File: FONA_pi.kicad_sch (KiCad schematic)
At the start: 2 parts, among them J1 Conn_01x20_Socket, J2 Conn_01x20_Socket

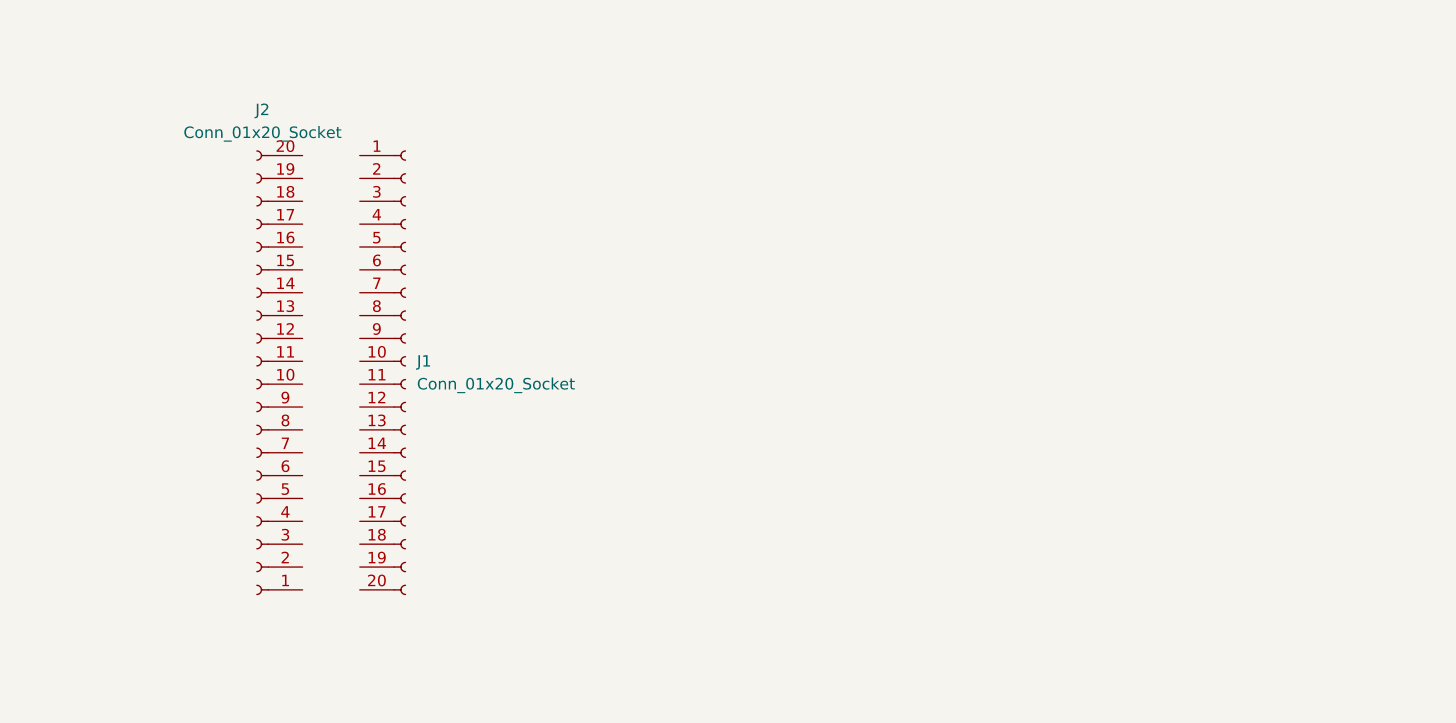
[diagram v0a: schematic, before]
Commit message: Added some 1x20 to schematic
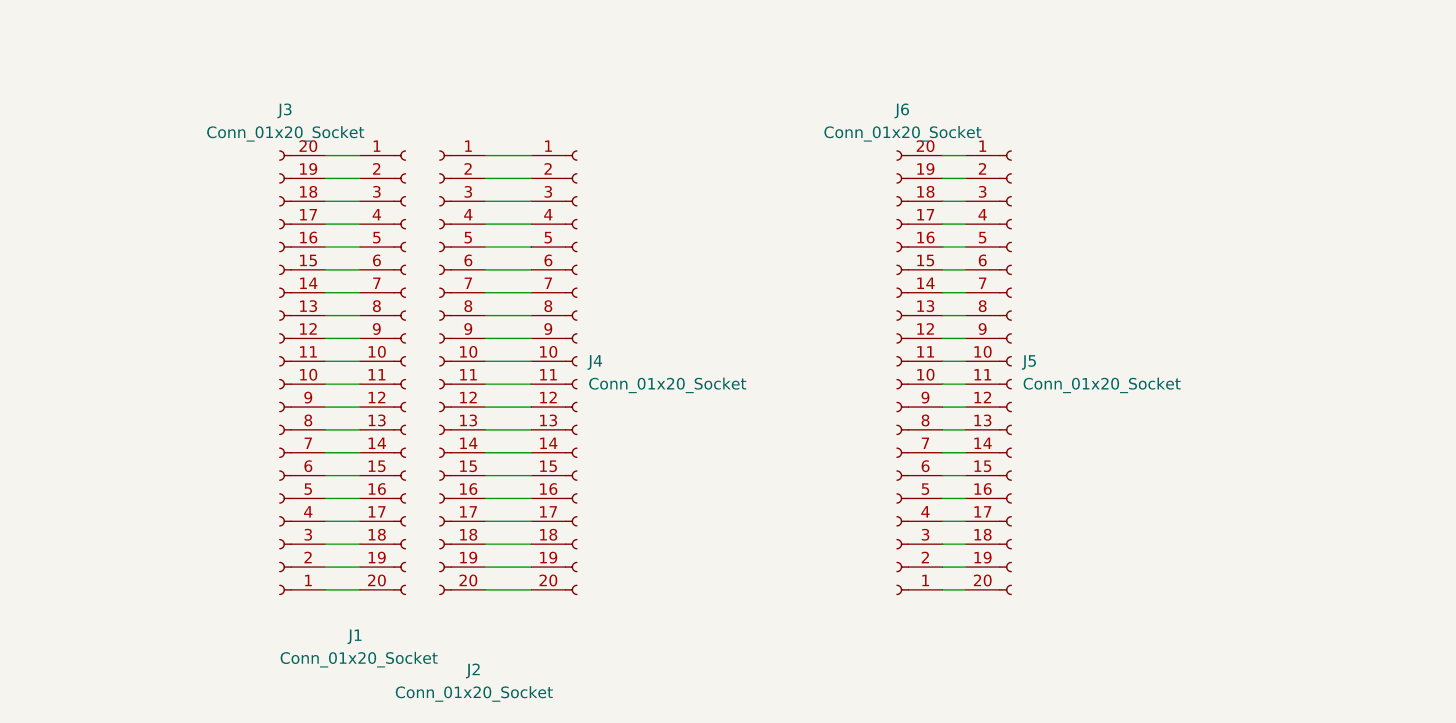
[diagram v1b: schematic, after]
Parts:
- added J3, J4, J5, J6: Conn_01x20_Socket, Connector_PinSocket_2.54mm:PinSocket_1x20_P2.54mm_Vertical, symbol Connector:Conn_01x20_Socket
- J1, J2: footprint (none) -> Connector_PinHeader_2.54mm:PinHeader_1x20_P2.54mm_Vertical
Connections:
- net at J2.1 (Pin_1): now also J4.1 (Pin_1)
- net at J2.10 (Pin_10): now also J4.10 (Pin_10)
- net at J2.11 (Pin_11): now also J4.11 (Pin_11)
- net at J2.12 (Pin_12): now also J4.12 (Pin_12)
- net at J2.13 (Pin_13): now also J4.13 (Pin_13)
- net at J2.14 (Pin_14): now also J4.14 (Pin_14)
- net at J2.15 (Pin_15): now also J4.15 (Pin_15)
- net at J2.16 (Pin_16): now also J4.16 (Pin_16)
- net at J2.17 (Pin_17): now also J4.17 (Pin_17)
- net at J2.18 (Pin_18): now also J4.18 (Pin_18)
- net at J2.19 (Pin_19): now also J4.19 (Pin_19)
- net at J2.2 (Pin_2): now also J4.2 (Pin_2)
- net at J2.20 (Pin_20): now also J4.20 (Pin_20)
- net at J2.3 (Pin_3): now also J4.3 (Pin_3)
- net at J2.4 (Pin_4): now also J4.4 (Pin_4)
- net at J2.5 (Pin_5): now also J4.5 (Pin_5)
- net at J2.6 (Pin_6): now also J4.6 (Pin_6)
- net at J2.7 (Pin_7): now also J4.7 (Pin_7)
- net at J2.8 (Pin_8): now also J4.8 (Pin_8)
- net at J2.9 (Pin_9): now also J4.9 (Pin_9)
- net at J1.1 (Pin_1): now also J3.20 (Pin_20)
- net at J1.10 (Pin_10): now also J3.11 (Pin_11)
- net at J1.11 (Pin_11): now also J3.10 (Pin_10)
- net at J1.12 (Pin_12): now also J3.9 (Pin_9)
- net at J1.13 (Pin_13): now also J3.8 (Pin_8)
- net at J1.14 (Pin_14): now also J3.7 (Pin_7)
- net at J1.15 (Pin_15): now also J3.6 (Pin_6)
- net at J1.16 (Pin_16): now also J3.5 (Pin_5)
- net at J1.17 (Pin_17): now also J3.4 (Pin_4)
- net at J1.18 (Pin_18): now also J3.3 (Pin_3)
- net at J1.19 (Pin_19): now also J3.2 (Pin_2)
- net at J1.2 (Pin_2): now also J3.19 (Pin_19)
- net at J1.20 (Pin_20): now also J3.1 (Pin_1)
- net at J1.3 (Pin_3): now also J3.18 (Pin_18)
- net at J1.4 (Pin_4): now also J3.17 (Pin_17)
- net at J1.5 (Pin_5): now also J3.16 (Pin_16)
- net at J1.6 (Pin_6): now also J3.15 (Pin_15)
- net at J1.7 (Pin_7): now also J3.14 (Pin_14)
- net at J1.8 (Pin_8): now also J3.13 (Pin_13)
- net at J1.9 (Pin_9): now also J3.12 (Pin_12)
- new net: J5.20 (Pin_20), J6.1 (Pin_1)
- new net: J5.11 (Pin_11), J6.10 (Pin_10)
- new net: J5.10 (Pin_10), J6.11 (Pin_11)
- new net: J5.9 (Pin_9), J6.12 (Pin_12)
- new net: J5.8 (Pin_8), J6.13 (Pin_13)
- new net: J5.7 (Pin_7), J6.14 (Pin_14)
- new net: J5.6 (Pin_6), J6.15 (Pin_15)
- new net: J5.5 (Pin_5), J6.16 (Pin_16)
- new net: J5.4 (Pin_4), J6.17 (Pin_17)
- new net: J5.3 (Pin_3), J6.18 (Pin_18)
- new net: J5.2 (Pin_2), J6.19 (Pin_19)
- new net: J5.19 (Pin_19), J6.2 (Pin_2)
- new net: J5.1 (Pin_1), J6.20 (Pin_20)
- new net: J5.18 (Pin_18), J6.3 (Pin_3)
- new net: J5.17 (Pin_17), J6.4 (Pin_4)
- new net: J5.16 (Pin_16), J6.5 (Pin_5)
- new net: J5.15 (Pin_15), J6.6 (Pin_6)
- new net: J5.14 (Pin_14), J6.7 (Pin_7)
- new net: J5.13 (Pin_13), J6.8 (Pin_8)
- new net: J5.12 (Pin_12), J6.9 (Pin_9)
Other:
- moved on the sheet: J2

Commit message: connections for pi and fona
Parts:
- added J7: Conn_01x20_Socket, Connector_PinHeader_2.00mm:PinHeader_1x20_P2.00mm_Vertical, symbol Connector:Conn_01x20_Socket
- J3: value Conn_01x20_Socket -> Outer_Pi_01x20_Socket
- J4: value Conn_01x20_Socket -> Inner_Pi_01x20_Socket
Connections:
- net at J5.20 (Pin_20), J6.1 (Pin_1): now also J7.1 (Pin_1)
- net at J5.11 (Pin_11), J6.10 (Pin_10): now also J7.10 (Pin_10)
- net at J5.10 (Pin_10), J6.11 (Pin_11): now also J7.11 (Pin_11)
- net at J5.9 (Pin_9), J6.12 (Pin_12): now also J7.12 (Pin_12)
- net at J5.8 (Pin_8), J6.13 (Pin_13): now also J7.13 (Pin_13)
- net at J5.7 (Pin_7), J6.14 (Pin_14): now also J7.14 (Pin_14)
- net at J5.6 (Pin_6), J6.15 (Pin_15): now also J7.15 (Pin_15)
- net at J5.5 (Pin_5), J6.16 (Pin_16): now also J7.16 (Pin_16)
- net at J5.4 (Pin_4), J6.17 (Pin_17): now also J7.17 (Pin_17)
- net at J5.3 (Pin_3), J6.18 (Pin_18): now also J7.18 (Pin_18)
- net at J5.2 (Pin_2), J6.19 (Pin_19): now also J7.19 (Pin_19)
- net at J5.19 (Pin_19), J6.2 (Pin_2): now also J7.2 (Pin_2)
- net at J5.1 (Pin_1), J6.20 (Pin_20): now also J7.20 (Pin_20)
- net at J5.18 (Pin_18), J6.3 (Pin_3): now also J7.3 (Pin_3)
- net at J5.17 (Pin_17), J6.4 (Pin_4): now also J7.4 (Pin_4)
- net at J5.16 (Pin_16), J6.5 (Pin_5): now also J7.5 (Pin_5)
- net at J5.15 (Pin_15), J6.6 (Pin_6): now also J7.6 (Pin_6)
- net at J5.14 (Pin_14), J6.7 (Pin_7): now also J7.7 (Pin_7)
- net at J5.13 (Pin_13), J6.8 (Pin_8): now also J7.8 (Pin_8)
- net at J5.12 (Pin_12), J6.9 (Pin_9): now also J7.9 (Pin_9)

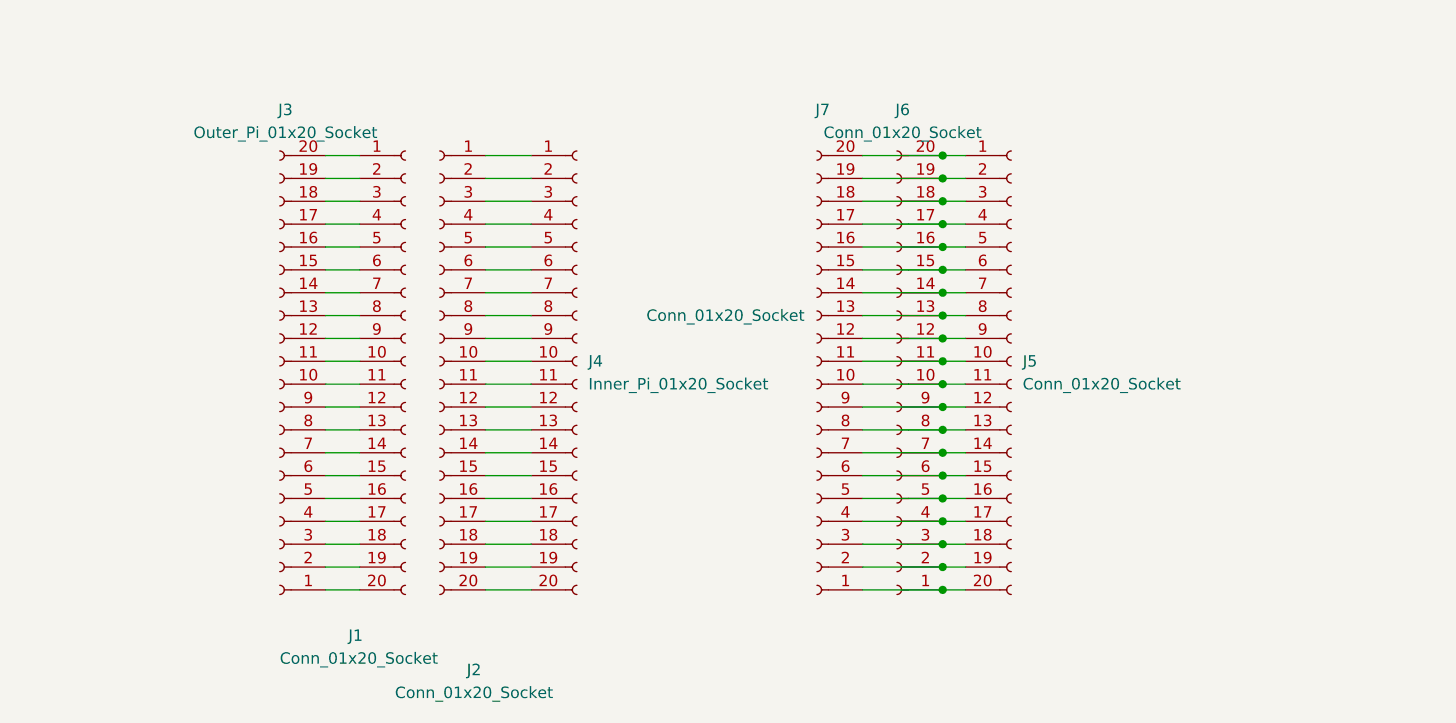
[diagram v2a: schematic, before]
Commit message: Flipped all the sockets so the pins are all aligned the same with square holes at the top, sch and pcb
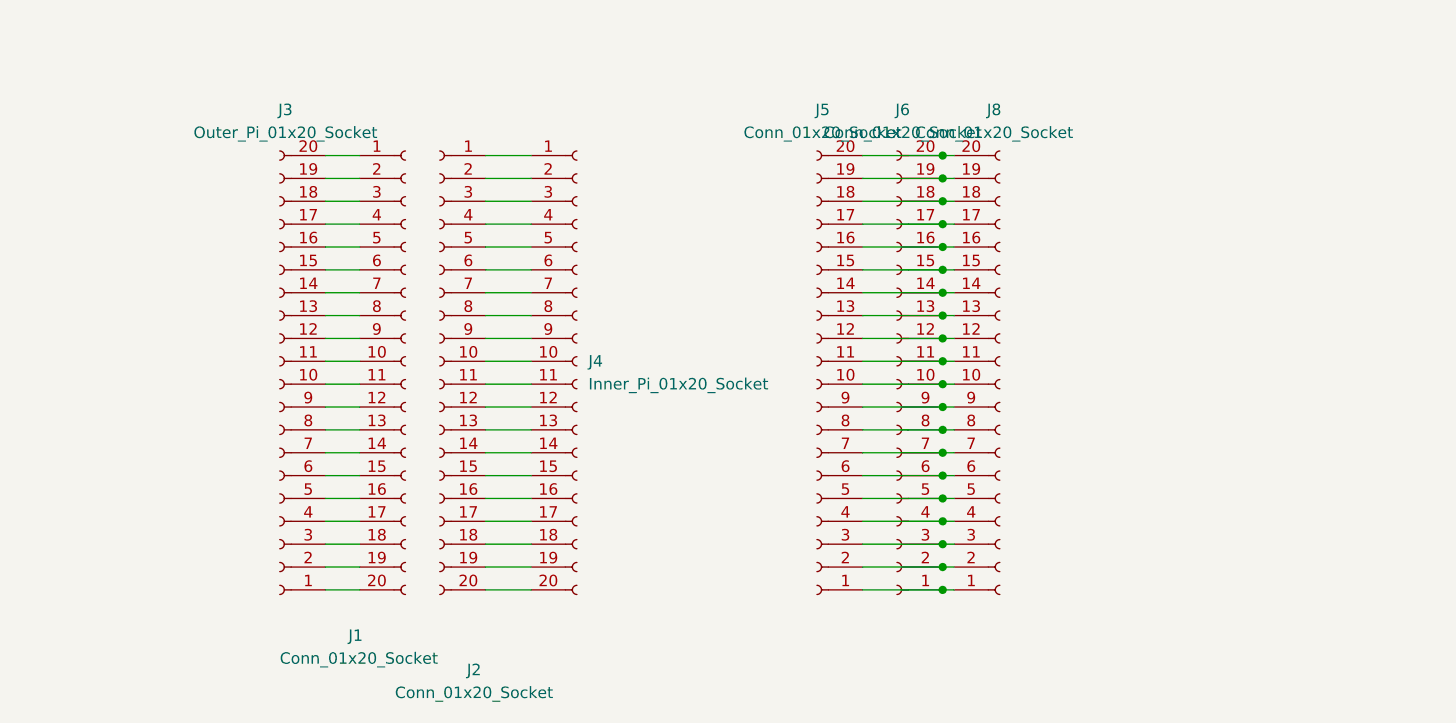
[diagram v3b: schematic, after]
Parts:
- removed J7: Conn_01x20_Socket, Connector_PinHeader_2.00mm:PinHeader_1x20_P2.00mm_Vertical, symbol Connector:Conn_01x20_Socket
- added J8: Conn_01x20_Socket, Connector_PinHeader_2.54mm:PinHeader_1x20_P2.54mm_Vertical, symbol Connector:Conn_01x20_Socket
- J5: footprint Connector_PinSocket_2.54mm:PinSocket_1x20_P2.54mm_Vertical -> Connector_PinHeader_2.54mm:PinHeader_1x20_P2.54mm_Vertical
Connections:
- net at J6.1 (Pin_1): now also J5.1 (Pin_1), J8.1 (Pin_1); no longer J5.20 (Pin_20)
- net at J6.10 (Pin_10): now also J5.10 (Pin_10), J8.10 (Pin_10); no longer J5.11 (Pin_11)
- net at J6.11 (Pin_11): now also J5.11 (Pin_11), J8.11 (Pin_11); no longer J5.10 (Pin_10)
- net at J6.12 (Pin_12): now also J5.12 (Pin_12), J8.12 (Pin_12); no longer J5.9 (Pin_9)
- net at J6.13 (Pin_13): now also J5.13 (Pin_13), J8.13 (Pin_13); no longer J5.8 (Pin_8)
- net at J6.14 (Pin_14): now also J5.14 (Pin_14), J8.14 (Pin_14); no longer J5.7 (Pin_7)
- net at J6.15 (Pin_15): now also J5.15 (Pin_15), J8.15 (Pin_15); no longer J5.6 (Pin_6)
- net at J6.16 (Pin_16): now also J5.16 (Pin_16), J8.16 (Pin_16); no longer J5.5 (Pin_5)
- net at J6.17 (Pin_17): now also J5.17 (Pin_17), J8.17 (Pin_17); no longer J5.4 (Pin_4)
- net at J6.18 (Pin_18): now also J5.18 (Pin_18), J8.18 (Pin_18); no longer J5.3 (Pin_3)
- net at J6.19 (Pin_19): now also J5.19 (Pin_19), J8.19 (Pin_19); no longer J5.2 (Pin_2)
- net at J6.2 (Pin_2): now also J5.2 (Pin_2), J8.2 (Pin_2); no longer J5.19 (Pin_19)
- net at J6.20 (Pin_20): now also J5.20 (Pin_20), J8.20 (Pin_20); no longer J5.1 (Pin_1)
- net at J6.3 (Pin_3): now also J5.3 (Pin_3), J8.3 (Pin_3); no longer J5.18 (Pin_18)
- net at J6.4 (Pin_4): now also J5.4 (Pin_4), J8.4 (Pin_4); no longer J5.17 (Pin_17)
- net at J6.5 (Pin_5): now also J5.5 (Pin_5), J8.5 (Pin_5); no longer J5.16 (Pin_16)
- net at J6.6 (Pin_6): now also J5.6 (Pin_6), J8.6 (Pin_6); no longer J5.15 (Pin_15)
- net at J6.7 (Pin_7): now also J5.7 (Pin_7), J8.7 (Pin_7); no longer J5.14 (Pin_14)
- net at J6.8 (Pin_8): now also J5.8 (Pin_8), J8.8 (Pin_8); no longer J5.13 (Pin_13)
- net at J6.9 (Pin_9): now also J5.9 (Pin_9), J8.9 (Pin_9); no longer J5.12 (Pin_12)

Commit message: Got rid of the headers in 3D viewer.  Cleaned up pin headers.  Using 40-pin Rpi header
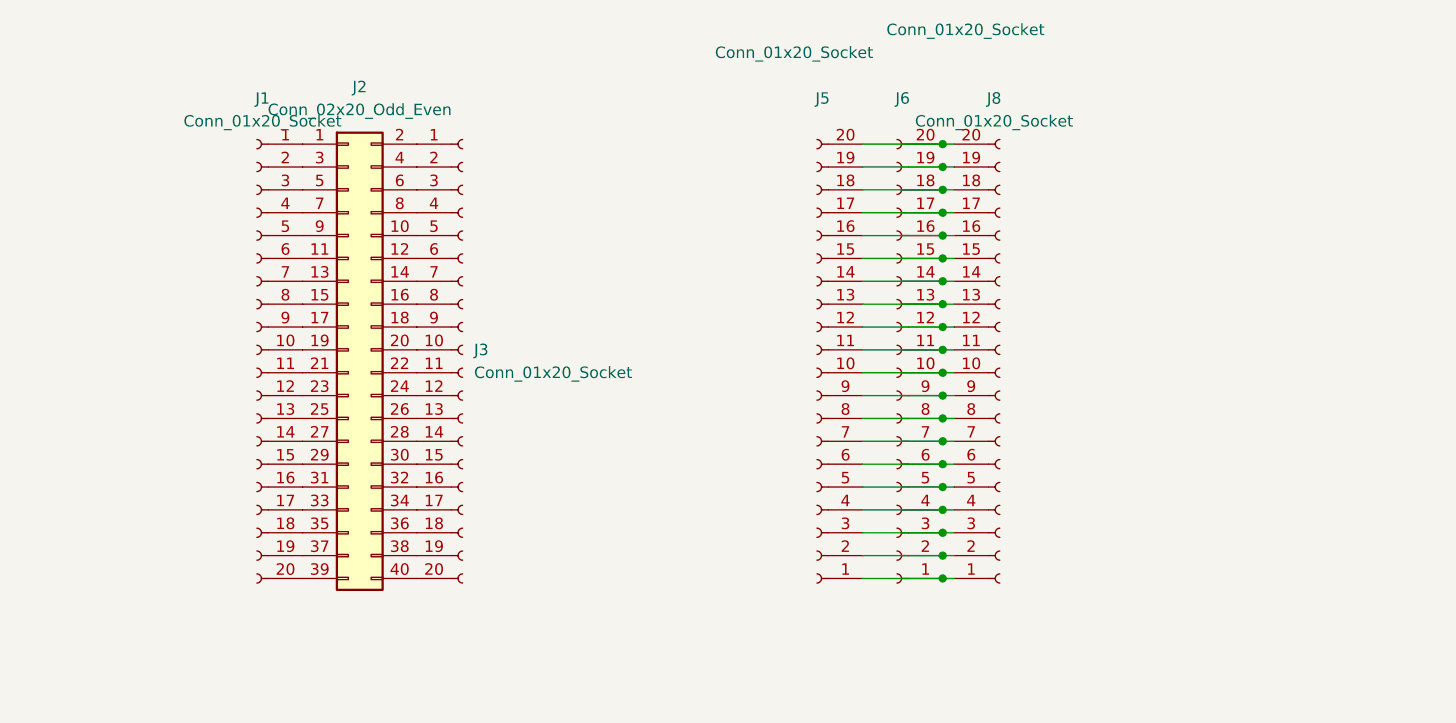
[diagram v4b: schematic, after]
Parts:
- removed J2: Conn_01x20_Socket, Connector_PinHeader_2.54mm:PinHeader_1x20_P2.54mm_Vertical, symbol Connector:Conn_01x20_Socket
- removed J4: Inner_Pi_01x20_Socket, Connector_PinSocket_2.54mm:PinSocket_1x20_P2.54mm_Vertical, symbol Connector:Conn_01x20_Socket
- added J2: Conn_02x20_Odd_Even, Connector_PinSocket_2.54mm:PinSocket_2x20_P2.54mm_Vertical, symbol Connector_Generic:Conn_02x20_Odd_Even
- J1, J5, J8: footprint Connector_PinHeader_2.54mm:PinHeader_1x20_P2.54mm_Vertical -> Connector_PinSocket_2.54mm:PinSocket_1x20_P2.54mm_Vertical
- J3: value Outer_Pi_01x20_Socket -> Conn_01x20_Socket
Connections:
- net at J1.1 (Pin_1): now also J2.1 (Pin_1); no longer J3.20 (Pin_20)
- net at J1.10 (Pin_10): now also J2.19 (Pin_19); no longer J3.11 (Pin_11)
- net at J3.10 (Pin_10): now also J2.20 (Pin_20); no longer J1.11 (Pin_11)
- net at J3.9 (Pin_9): now also J2.18 (Pin_18); no longer J1.12 (Pin_12)
- net at J3.8 (Pin_8): now also J2.16 (Pin_16); no longer J1.13 (Pin_13)
- net at J3.7 (Pin_7): now also J2.14 (Pin_14); no longer J1.14 (Pin_14)
- net at J3.6 (Pin_6): now also J2.12 (Pin_12); no longer J1.15 (Pin_15)
- net at J3.5 (Pin_5): now also J2.10 (Pin_10); no longer J1.16 (Pin_16)
- net at J1.17 (Pin_17): now also J2.33 (Pin_33); no longer J3.4 (Pin_4)
- net at J1.18 (Pin_18): now also J2.35 (Pin_35); no longer J3.3 (Pin_3)
- net at J1.19 (Pin_19): now also J2.37 (Pin_37); no longer J3.2 (Pin_2)
- net at J1.2 (Pin_2): now also J2.3 (Pin_3); no longer J3.19 (Pin_19)
- net at J3.1 (Pin_1): now also J2.2 (Pin_2); no longer J1.20 (Pin_20)
- net at J3.18 (Pin_18): now also J2.36 (Pin_36); no longer J1.3 (Pin_3)
- net at J3.17 (Pin_17): now also J2.34 (Pin_34); no longer J1.4 (Pin_4)
- net at J3.16 (Pin_16): now also J2.32 (Pin_32); no longer J1.5 (Pin_5)
- net at J1.6 (Pin_6): now also J2.11 (Pin_11); no longer J3.15 (Pin_15)
- net at J1.7 (Pin_7): now also J2.13 (Pin_13); no longer J3.14 (Pin_14)
- net at J1.8 (Pin_8): now also J2.15 (Pin_15); no longer J3.13 (Pin_13)
- net at J1.9 (Pin_9): now also J2.17 (Pin_17); no longer J3.12 (Pin_12)
- new net: J1.11 (Pin_11), J2.21 (Pin_21)
- new net: J2.22 (Pin_22), J3.11 (Pin_11)
- new net: J1.12 (Pin_12), J2.23 (Pin_23)
- new net: J2.24 (Pin_24), J3.12 (Pin_12)
- new net: J1.13 (Pin_13), J2.25 (Pin_25)
- new net: J2.26 (Pin_26), J3.13 (Pin_13)
- new net: J1.14 (Pin_14), J2.27 (Pin_27)
- new net: J2.28 (Pin_28), J3.14 (Pin_14)
- new net: J1.15 (Pin_15), J2.29 (Pin_29)
- new net: J2.30 (Pin_30), J3.15 (Pin_15)
- new net: J1.16 (Pin_16), J2.31 (Pin_31)
- new net: J2.38 (Pin_38), J3.19 (Pin_19)
- new net: J1.20 (Pin_20), J2.39 (Pin_39)
- new net: J2.4 (Pin_4), J3.2 (Pin_2)
- new net: J2.40 (Pin_40), J3.20 (Pin_20)
- new net: J1.3 (Pin_3), J2.5 (Pin_5)
- new net: J2.6 (Pin_6), J3.3 (Pin_3)
- new net: J1.4 (Pin_4), J2.7 (Pin_7)
- new net: J2.8 (Pin_8), J3.4 (Pin_4)
- new net: J1.5 (Pin_5), J2.9 (Pin_9)
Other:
- moved on the sheet: J5, J6, J8
